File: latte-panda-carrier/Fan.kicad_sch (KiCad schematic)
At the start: 0 parts

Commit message: 120.1
CPU fan
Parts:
- added C84, C85: 100nF/50V, A_HDJ_Library:C_0402_1005Metric, symbol Device:C
- added D26, D27: 1N5819WS, A_HDJ_Library:D_SOD-323, symbol Diode:1N5819WS
- added JP2: SolderJumper_2_Open, Jumper:SolderJumper-2_P1.3mm_Open_RoundedPad1.0x1.5mm, symbol Jumper:SolderJumper_2_Open
- added M1, M2: Fan_4pin, A_HDJ_Library:JST_PH_B4B-PH-K_1x04_P2.00mm_Vertical, symbol Motor:Fan_4pin
- added R63: 10K/1%, A_HDJ_Library:R_0402_1005Metric, symbol Device:R
- added R64, R65, R72, R74, R75: 4.7K/1%, A_HDJ_Library:R_0402_1005Metric, symbol Device:R
- added R66, R67: 21.5K/1%, A_HDJ_Library:R_0402_1005Metric, symbol Device:R
- added R68, R70: 21.5K/1%, symbol Device:R
- added R69, R71: 100R/1%, A_HDJ_Library:R_0402_1005Metric, symbol Device:R
- added R73: 0R/1%, A_HDJ_Library:R_0402_1005Metric, symbol Device:R
- added TH1: NTC_Test, A_HDJ_Library:R_0603_1608Metric, symbol Device:Thermistor_NTC
- added TP11, TP12: TestPoint, symbol Connector:TestPoint
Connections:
- new net: D27.2 (A), M2.3 (Tacho), R70.1, R74.1
- new net: C85.1, D27.1 (K), M2.2 (+), R73.1, R74.2, R75.1
- new net: JP2.2 (B), R63.2, TH1.1
- new net: D26.2 (A), M1.3 (Tacho), R68.1, R72.1
- new net: M2.4 (PWM), R71.1
- new net: M1.4 (PWM), R69.1
- new net +12V: R75.2
- new net +3V3: R63.1, R64.1, R65.1
- new net +5V: C84.1, D26.1 (K), M1.2 (+), R72.2, R73.2
- new net FAN_1_PWM: R64.2, R69.2, TP12.1
- new net FAN_1_TAC: R66.1, R68.2, TP11.1
- new net FAN_2_PWM: R65.2, R71.2
- new net FAN_2_TAC: R67.1, R70.2
- new net GND: C84.2, C85.2, M1.1 (-), M2.1 (-), R66.2, R67.2, TH1.2
- new net TEMP: JP2.1 (A)
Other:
- note added: "CPU Fan"
- note added: "LattePanda Mu has integrated pull-ups"
- note added: "Reserved for 12V fan FAN_TAC input only allows 3.3V level"
- note added: "SYS Fan"

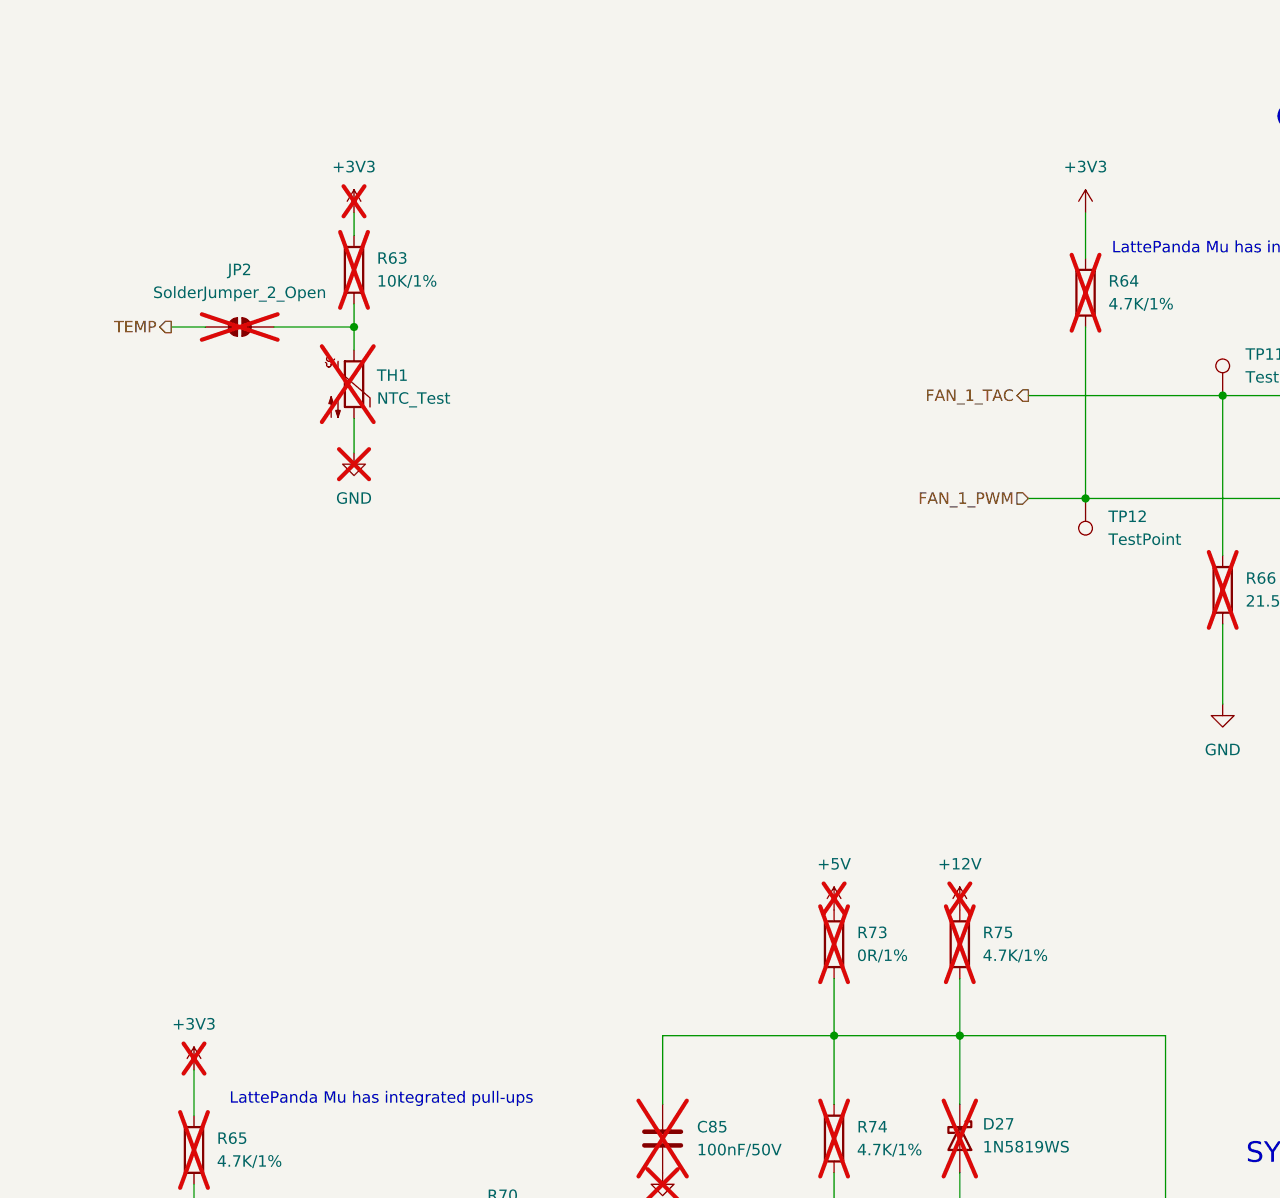
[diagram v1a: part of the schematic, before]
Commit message: 120.2
Wire CPU fan on root sheet and fix 2 power net name problems (+3V3 symbols
changed to +3.3V)
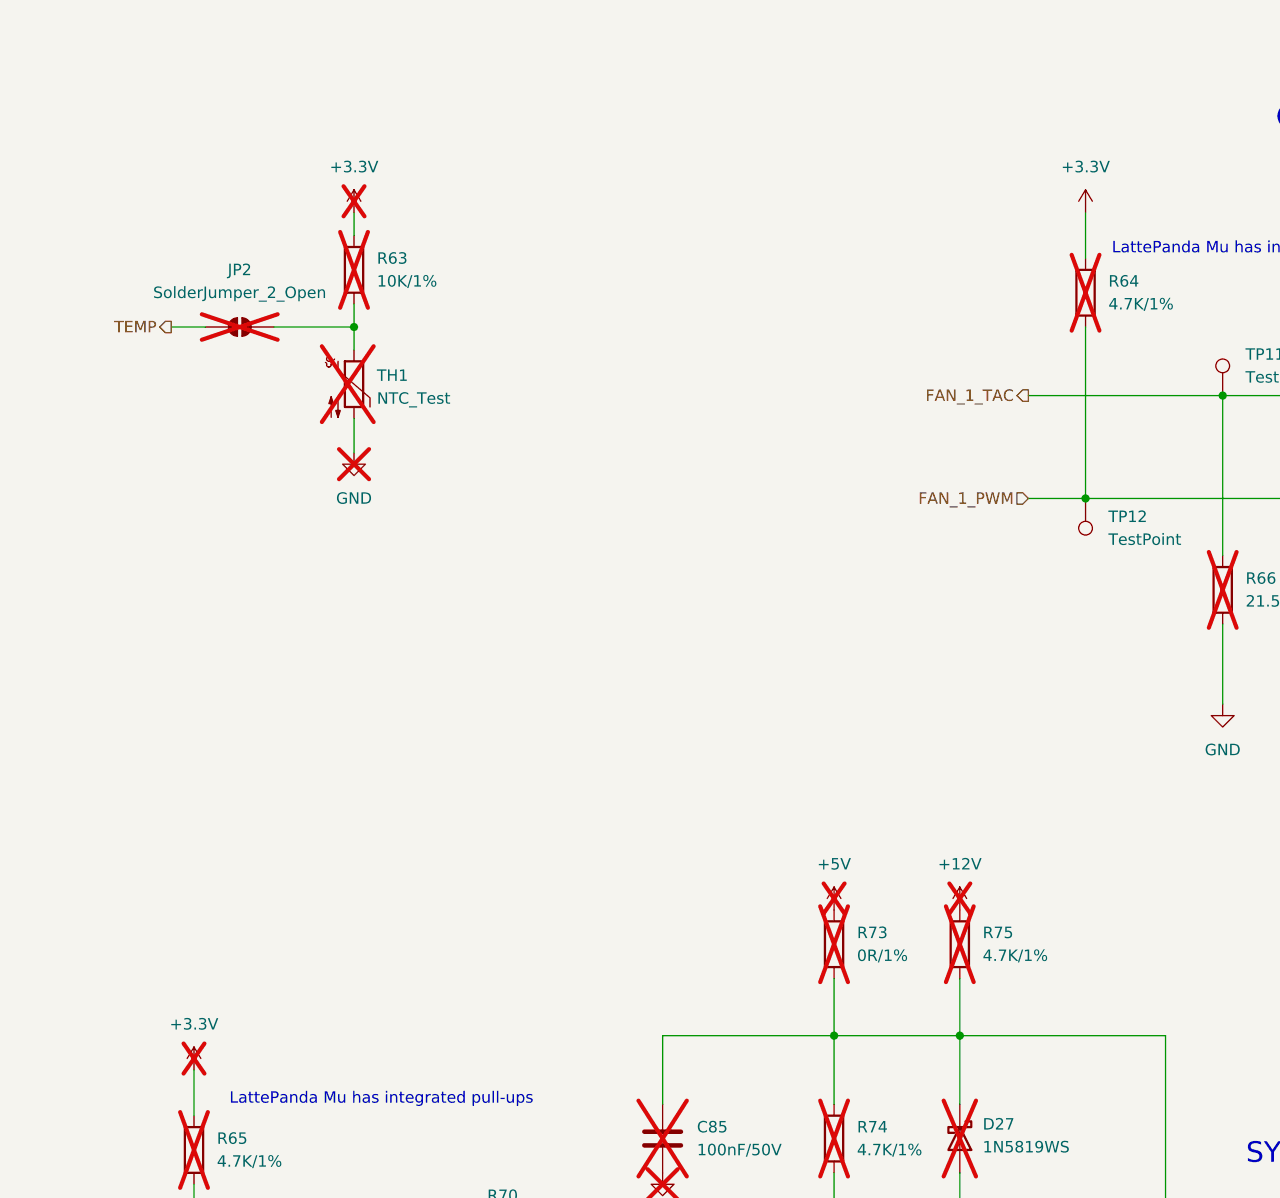
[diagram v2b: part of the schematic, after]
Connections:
- net +3V3 renamed +3.3V
